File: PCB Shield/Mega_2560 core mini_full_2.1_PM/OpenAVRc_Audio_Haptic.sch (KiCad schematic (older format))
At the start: 13 parts, among them P22 JQ6500_28P, P27 HP, P5 Vibreur, P8 Audio

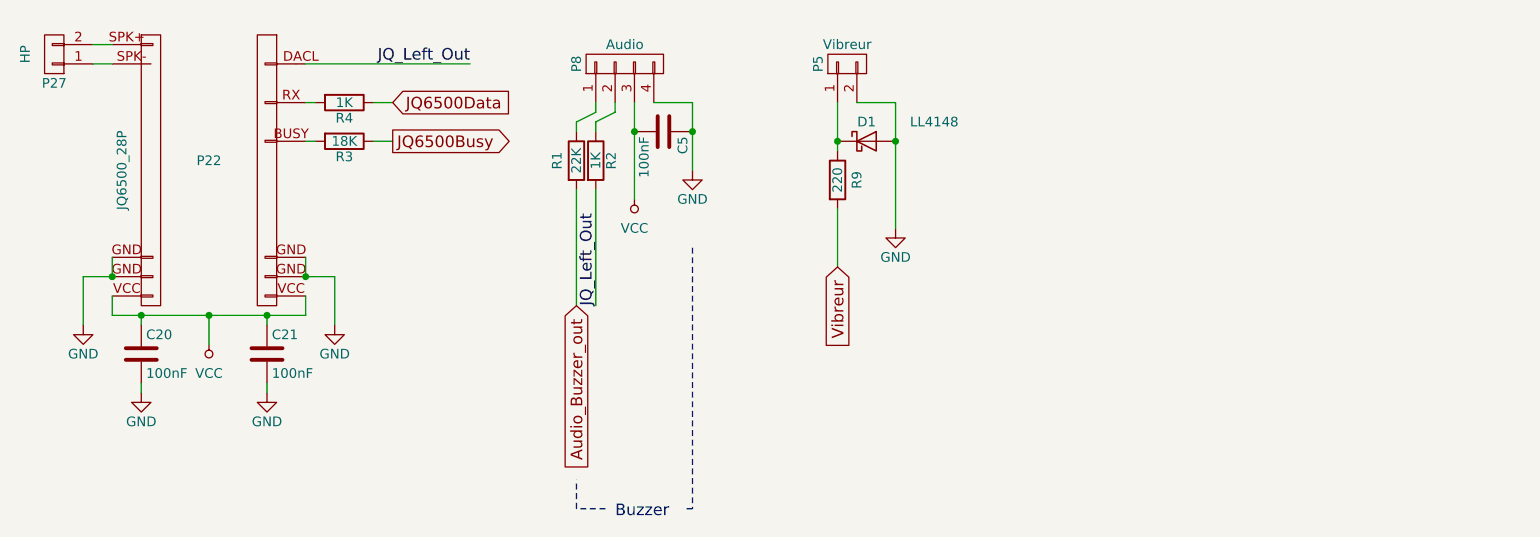
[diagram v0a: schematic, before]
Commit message: Update pcb files
update haptic pcb.
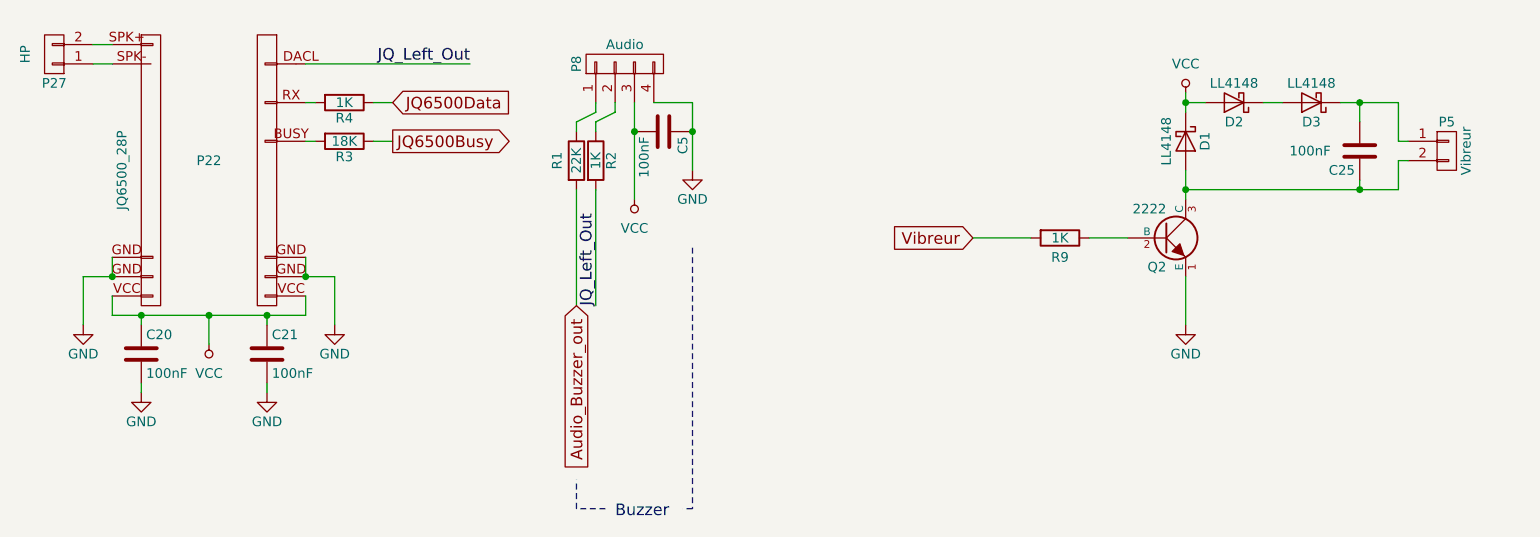
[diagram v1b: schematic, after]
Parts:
- added C25: 100nF, Capacitors_SMD:C_1206, symbol C-RESCUE-Mega_2560_core_mini_full_2.0
- added D2, D3: LL4148, Diodes_SMD:D_SOD-123, symbol MBR0520
- added Q2: 2222, symbol NPN
- R9: value 220 -> 1K
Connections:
- net GND: now also Q2.1 (E); no longer D1.2 (A), P5.2 (P2)
- net VCC: now also D1.1 (K), D2.2 (A)
- new net: C25.2, D3.1 (K), P5.1 (P1)
- new net: C25.1, D1.2 (A), P5.2 (P2), Q2.3 (C)
- new net: Q2.2 (B), R9.1
- new net: D2.1 (K), D3.2 (A)
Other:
- moved on the sheet: D1, P5, R9
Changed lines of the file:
@@
 Sheet 6 7
 Title "Shield Mega2560 core Full"
-Date "2018-02-28"
+Date "2018-03-01"
 Rev "2.10"
 Comp "© Team OpenAVRc"
@@
 L CONN_01X02 P5
 U 1 1 59C5A561
-P 7300 3050
-F 0 "P5" H 7300 3200 50  0000 C CNN
-F 1 "Vibreur" V 7400 3050 50  0000 C CNN
-F 2 "Pin_Headers:Pin_Header_Straight_1x02_Pitch2.54mm" H 7300 3050 50  0001 C CNN
-F 3 "" H 7300 3050 50  0000 C CNN
-	1    7300 3050
-	0    -1   -1   0
-$EndComp
-$Comp
-L GND-RESCUE-Mega_2560_core_mini_full_2.0 #PWR0105
-U 1 1 59C5A568
-P 7550 3900
-F 0 "#PWR0105" H 7550 3650 50  0001 C CNN
-F 1 "GND" H 7550 3750 50  0000 C CNN
-F 2 "" H 7550 3900 50  0000 C CNN
-F 3 "" H 7550 3900 50  0000 C CNN
-	1    7550 3900
+P 10400 3500
+F 0 "P5" H 10400 3650 50  0000 C CNN
+F 1 "Vibreur" V 10500 3500 50  0000 C CNN
+F 2 "Pin_Headers:Pin_Header_Straight_1x02_Pitch2.54mm" H 10400 3500 50  0001 C CNN
+F 3 "" H 10400 3500 50  0000 C CNN
+	1    10400 3500
 	1    0    0    -1
 $EndComp
@@
 $EndComp
 $Comp
-L VCC #PWR0106
+L VCC #PWR0105
 U 1 1 59C5A58E
 P 4000 4500
-F 0 "#PWR0106" H 4000 4350 50  0001 C CNN
+F 0 "#PWR0105" H 4000 4350 50  0001 C CNN
 F 1 "VCC" H 4000 4650 50  0000 C CNN
 F 2 "" H 4000 4500 50  0000 C CNN
@@
 $EndComp
 $Comp
-L GND-RESCUE-Mega_2560_core_mini_full_2.0 #PWR0107
+L GND-RESCUE-Mega_2560_core_mini_full_2.0 #PWR0106
 U 1 1 59C5A594
 P 3350 4400
-F 0 "#PWR0107" H 3350 4150 50  0001 C CNN
+F 0 "#PWR0106" H 3350 4150 50  0001 C CNN
 F 1 "GND" H 3350 4250 50  0000 C CNN
 F 2 "" H 3350 4400 50  0000 C CNN
@@
 $EndComp
 $Comp
-L GND-RESCUE-Mega_2560_core_mini_full_2.0 #PWR0108
+L GND-RESCUE-Mega_2560_core_mini_full_2.0 #PWR0107
 U 1 1 59C5A59A
 P 4650 4400
-F 0 "#PWR0108" H 4650 4150 50  0001 C CNN
+F 0 "#PWR0107" H 4650 4150 50  0001 C CNN
 F 1 "GND" H 4650 4250 50  0000 C CNN
 F 2 "" H 4650 4400 50  0000 C CNN
@@
 L MBR0520 D1
 U 1 1 59C5A5A7
-P 7400 3450
-F 0 "D1" H 7400 3550 50  0000 C CNN
-F 1 "LL4148" H 7750 3550 50  0000 C CNN
-F 2 "Diodes_SMD:D_SOD-123" H 7400 3275 50  0001 C CNN
-F 3 "" H 7400 3450 50  0001 C CNN
-	1    7400 3450
-	1    0    0    -1
+P 9050 3450
+F 0 "D1" H 9050 3550 50  0000 C CNN
+F 1 "LL4148" H 9050 3350 50  0000 C CNN
+F 2 "Diodes_SMD:D_SOD-123" H 9050 3275 50  0001 C CNN
+F 3 "" H 9050 3450 50  0001 C CNN
+	1    9050 3450
+	0    1    1    0
 $EndComp
 $Comp
 L R-RESCUE-Mega_2560_core_mini_full_2.0 R9
 U 1 1 59C5A5AE
-P 7250 3650
-F 0 "R9" V 7350 3650 50  0000 C CNN
-F 1 "220" V 7250 3650 50  0000 C CNN
-F 2 "anthoperso:R_1206" V 7180 3650 50  0001 C CNN
-F 3 "" H 7250 3650 50  0000 C CNN
-	1    7250 3650
-	1    0    0    -1
+P 8400 3950
+F 0 "R9" V 8500 3950 50  0000 C CNN
+F 1 "1K" V 8400 3950 50  0000 C CNN
+F 2 "anthoperso:R_1206" V 8330 3950 50  0001 C CNN
+F 3 "" H 8400 3950 50  0000 C CNN
+	1    8400 3950
+	0    1    1    0
 $EndComp
 $Comp
@@
 $EndComp
 $Comp
-L GND-RESCUE-Mega_2560_core_mini_full_2.0 #PWR0109
+L GND-RESCUE-Mega_2560_core_mini_full_2.0 #PWR0108
 U 1 1 59C5A5DF
 P 3650 4750
-F 0 "#PWR0109" H 3650 4500 50  0001 C CNN
+F 0 "#PWR0108" H 3650 4500 50  0001 C CNN
 F 1 "GND" H 3650 4600 50  0000 C CNN
 F 2 "" H 3650 4750 50  0000 C CNN
@@
 $EndComp
 $Comp
-L GND-RESCUE-Mega_2560_core_mini_full_2.0 #PWR0110
+L GND-RESCUE-Mega_2560_core_mini_full_2.0 #PWR0109
 U 1 1 59C5A5E5
 P 4300 4750
-F 0 "#PWR0110" H 4300 4500 50  0001 C CNN
+F 0 "#PWR0109" H 4300 4500 50  0001 C CNN
 F 1 "GND" H 4300 4600 50  0000 C CNN
 F 2 "" H 4300 4750 50  0000 C CNN
@@
 Wire Wire Line
 	6000 3700 6000 4300
-Connection ~ 7550 3450
-Wire Wire Line
-	7550 3250 7550 3900
-Wire Wire Line
-	7350 3250 7550 3250
 Connection ~ 6200 3400
 Connection ~ 6500 3400
@@
 	4500 3050 5350 3050
 Wire Wire Line
-	7250 3250 7250 3500
-Wire Wire Line
-	7250 3800 7250 4100
-Connection ~ 7250 3450
+	8250 3950 7950 3950
 Wire Wire Line
 	3400 3050 3500 3050
@@
 Text GLabel 4950 3450 2    60   Output ~ 0
 JQ6500Busy
-Text GLabel 7250 4100 3    60   Input ~ 0
+Text GLabel 7950 3950 0    60   Input ~ 0
 Vibreur
+$Comp
+L NPN Q2
+U 1 1 5A97FDE8
+P 8950 3950
+F 0 "Q2" H 8950 3800 50  0000 R CNN
+F 1 "2222" H 8950 4100 50  0000 R CNN
+F 2 "" H 8950 3950 60  0000 C CNN
+F 3 "" H 8950 3950 60  0000 C CNN
+	1    8950 3950
+	1    0    0    -1
+$EndComp
+Wire Wire Line
+	8550 3950 8750 3950
+$Comp
+L GND-RESCUE-Mega_2560_core_mini_full_2.0 #PWR0110
+U 1 1 5A9805CC
+P 9050 4400
+F 0 "#PWR0110" H 9050 4150 50  0001 C CNN
+F 1 "GND" H 9050 4250 50  0000 C CNN
+F 2 "" H 9050 4400 50  0000 C CNN
+F 3 "" H 9050 4400 50  0000 C CNN
+	1    9050 4400
+	1    0    0    -1
+$EndComp
+Wire Wire Line
+	9050 4150 9050 4400
+$Comp
+L C-RESCUE-Mega_2560_core_mini_full_2.0 C25
+U 1 1 5A980AA9
+P 9950 3500
+F 0 "C25" H 9975 3600 50  0000 L CNN
+F 1 "100nF" H 10100 3500 50  0000 L CNN
+F 2 "Capacitors_SMD:C_1206" H 9988 3350 50  0001 C CNN
+F 3 "" H 9950 3500 50  0000 C CNN
+	1    9950 3500
+	-1   0    0    1
+$EndComp
+$Comp
+L MBR0520 D2
+U 1 1 5A980F3A
+P 9300 3250
+F 0 "D2" H 9300 3350 50  0000 C CNN
+F 1 "LL4148" H 9300 3150 50  0000 C CNN
+F 2 "Diodes_SMD:D_SOD-123" H 9300 3075 50  0001 C CNN
+F 3 "" H 9300 3250 50  0001 C CNN
+	1    9300 3250
+	-1   0    0    1
+$EndComp
+$Comp
+L MBR0520 D3
+U 1 1 5A980F85
+P 9700 3250
+F 0 "D3" H 9700 3350 50  0000 C CNN
+F 1 "LL4148" H 9700 3150 50  0000 C CNN
+F 2 "Diodes_SMD:D_SOD-123" H 9700 3075 50  0001 C CNN
+F 3 "" H 9700 3250 50  0001 C CNN
+	1    9700 3250
+	-1   0    0    1
+$EndComp
+$Comp
+L VCC #PWR0111
+U 1 1 5A981097
+P 9050 3200
+F 0 "#PWR0111" H 9050 3050 50  0001 C CNN
+F 1 "VCC" H 9050 3350 50  0000 C CNN
+F 2 "" H 9050 3200 50  0000 C CNN
+F 3 "" H 9050 3200 50  0000 C CNN
+	1    9050 3200
+	1    0    0    -1
+$EndComp
+Wire Wire Line
+	9050 3200 9050 3300
+Wire Wire Line
+	9050 3750 9050 3600
+Wire Wire Line
+	9850 3250 10150 3250
+Wire Wire Line
+	9550 3250 9450 3250
+Wire Wire Line
+	9150 3250 9050 3250
+Connection ~ 9050 3250
+Wire Wire Line
+	10200 3450 10150 3450
+Wire Wire Line
+	10150 3450 10150 3250
+Wire Wire Line
+	9950 3350 9950 3250
+Connection ~ 9950 3250
+Wire Wire Line
+	10200 3550 10150 3550
+Wire Wire Line
+	10150 3550 10150 3700
+Wire Wire Line
+	10150 3700 9050 3700
+Connection ~ 9050 3700
+Wire Wire Line
+	9950 3650 9950 3700
+Connection ~ 9950 3700
 $EndSCHEMATC

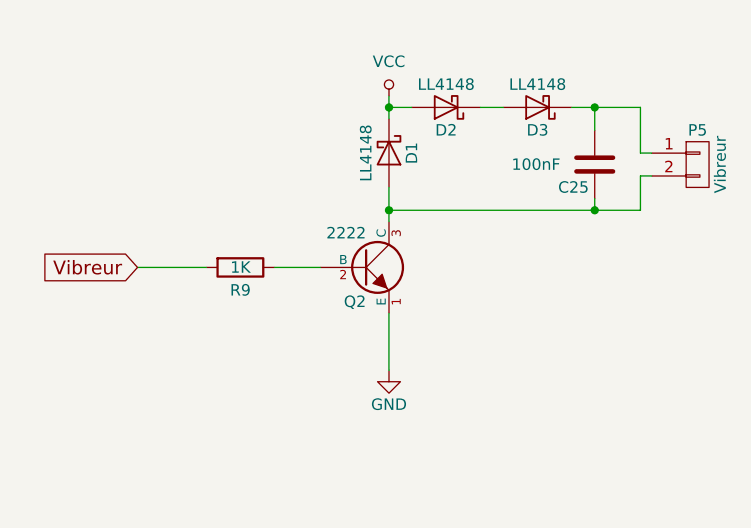
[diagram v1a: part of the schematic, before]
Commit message: Update schematic & pcb files
- modify pcb for haptic.
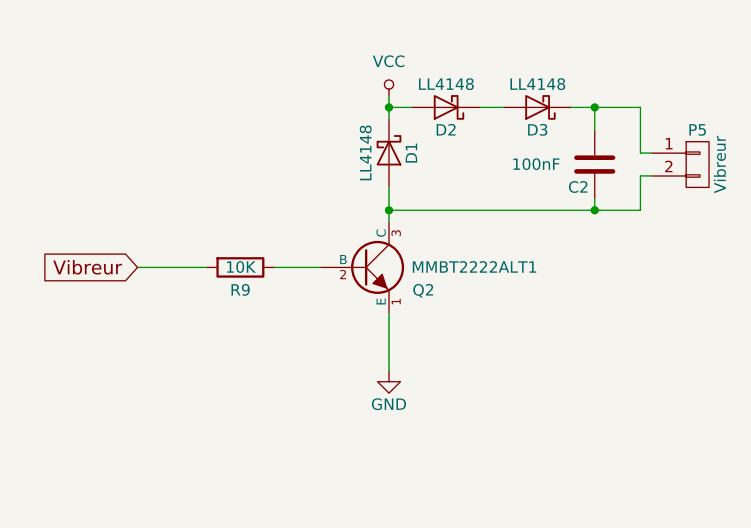
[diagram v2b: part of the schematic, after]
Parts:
- Q2: value 2222 -> MMBT2222ALT1
- R9: value 1K -> 10K
- renumbered C25 to C2
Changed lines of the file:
@@
 Sheet 6 7
 Title "Shield Mega2560 core Full"
-Date "2018-03-01"
+Date "2018-03-02"
 Rev "2.10"
 Comp "© Team OpenAVRc"
@@
 $EndDescr
 $Comp
-L GND-RESCUE-Mega_2560_core_mini_full_2.0 #PWR0103
+L GND-RESCUE-Mega_2560_core_mini_full_2.0 #PWR0102
 U 1 1 59C5A54C
 P 6500 3600
-F 0 "#PWR0103" H 6500 3350 50  0001 C CNN
+F 0 "#PWR0102" H 6500 3350 50  0001 C CNN
 F 1 "GND" H 6500 3450 50  0000 C CNN
 F 2 "" H 6500 3600 50  0000 C CNN
@@
 $EndComp
 $Comp
-L VCC #PWR0104
+L VCC #PWR0103
 U 1 1 59C5A552
 P 6200 3750
-F 0 "#PWR0104" H 6200 3600 50  0001 C CNN
+F 0 "#PWR0103" H 6200 3600 50  0001 C CNN
 F 1 "VCC" H 6200 3900 50  0000 C CNN
 F 2 "" H 6200 3750 50  0000 C CNN
@@
 $EndComp
 $Comp
-L VCC #PWR0105
+L VCC #PWR0104
 U 1 1 59C5A58E
 P 4000 4500
-F 0 "#PWR0105" H 4000 4350 50  0001 C CNN
+F 0 "#PWR0104" H 4000 4350 50  0001 C CNN
 F 1 "VCC" H 4000 4650 50  0000 C CNN
 F 2 "" H 4000 4500 50  0000 C CNN
@@
 $EndComp
 $Comp
-L GND-RESCUE-Mega_2560_core_mini_full_2.0 #PWR0106
+L GND-RESCUE-Mega_2560_core_mini_full_2.0 #PWR0105
 U 1 1 59C5A594
 P 3350 4400
-F 0 "#PWR0106" H 3350 4150 50  0001 C CNN
+F 0 "#PWR0105" H 3350 4150 50  0001 C CNN
 F 1 "GND" H 3350 4250 50  0000 C CNN
 F 2 "" H 3350 4400 50  0000 C CNN
@@
 $EndComp
 $Comp
-L GND-RESCUE-Mega_2560_core_mini_full_2.0 #PWR0107
+L GND-RESCUE-Mega_2560_core_mini_full_2.0 #PWR0106
 U 1 1 59C5A59A
 P 4650 4400
-F 0 "#PWR0107" H 4650 4150 50  0001 C CNN
+F 0 "#PWR0106" H 4650 4150 50  0001 C CNN
 F 1 "GND" H 4650 4250 50  0000 C CNN
 F 2 "" H 4650 4400 50  0000 C CNN
@@
 P 8400 3950
 F 0 "R9" V 8500 3950 50  0000 C CNN
-F 1 "1K" V 8400 3950 50  0000 C CNN
+F 1 "10K" V 8400 3950 50  0000 C CNN
 F 2 "anthoperso:R_1206" V 8330 3950 50  0001 C CNN
 F 3 "" H 8400 3950 50  0000 C CNN
@@
 $EndComp
 $Comp
-L GND-RESCUE-Mega_2560_core_mini_full_2.0 #PWR0108
+L GND-RESCUE-Mega_2560_core_mini_full_2.0 #PWR0107
 U 1 1 59C5A5DF
 P 3650 4750
-F 0 "#PWR0108" H 3650 4500 50  0001 C CNN
+F 0 "#PWR0107" H 3650 4500 50  0001 C CNN
 F 1 "GND" H 3650 4600 50  0000 C CNN
 F 2 "" H 3650 4750 50  0000 C CNN
@@
 $EndComp
 $Comp
-L GND-RESCUE-Mega_2560_core_mini_full_2.0 #PWR0109
+L GND-RESCUE-Mega_2560_core_mini_full_2.0 #PWR0108
 U 1 1 59C5A5E5
 P 4300 4750
-F 0 "#PWR0109" H 4300 4500 50  0001 C CNN
+F 0 "#PWR0108" H 4300 4500 50  0001 C CNN
 F 1 "GND" H 4300 4600 50  0000 C CNN
 F 2 "" H 4300 4750 50  0000 C CNN
 F 3 "" H 4300 4750 50  0000 C CNN
 	1    4300 4750
+	1    0    0    -1
+$EndComp
+Text GLabel 5900 4300 3    60   Input ~ 0
+Audio_Buzzer_out
+Text GLabel 4950 3250 2    60   Input ~ 0
+JQ6500Data
+Text GLabel 4950 3450 2    60   Output ~ 0
+JQ6500Busy
+Text GLabel 7950 3950 0    60   Input ~ 0
+Vibreur
+$Comp
+L NPN Q2
+U 1 1 5A97FDE8
+P 8950 3950
+F 0 "Q2" H 9250 3850 50  0000 R CNN
+F 1 "MMBT2222ALT1" H 9700 3950 50  0000 R CNN
+F 2 "" H 8950 3950 60  0000 C CNN
+F 3 "" H 8950 3950 60  0000 C CNN
+	1    8950 3950
+	1    0    0    -1
+$EndComp
+$Comp
+L GND-RESCUE-Mega_2560_core_mini_full_2.0 #PWR0109
+U 1 1 5A9805CC
+P 9050 4400
+F 0 "#PWR0109" H 9050 4150 50  0001 C CNN
+F 1 "GND" H 9050 4250 50  0000 C CNN
+F 2 "" H 9050 4400 50  0000 C CNN
+F 3 "" H 9050 4400 50  0000 C CNN
+	1    9050 4400
+	1    0    0    -1
+$EndComp
+$Comp
+L C-RESCUE-Mega_2560_core_mini_full_2.0 C2
+U 1 1 5A980AA9
+P 9950 3500
+F 0 "C2" H 9975 3600 50  0000 L CNN
+F 1 "100nF" H 10100 3500 50  0000 L CNN
+F 2 "Capacitors_SMD:C_1206" H 9988 3350 50  0001 C CNN
+F 3 "" H 9950 3500 50  0000 C CNN
+	1    9950 3500
+	-1   0    0    1
+$EndComp
+$Comp
+L MBR0520 D2
+U 1 1 5A980F3A
+P 9300 3250
+F 0 "D2" H 9300 3350 50  0000 C CNN
+F 1 "LL4148" H 9300 3150 50  0000 C CNN
+F 2 "Diodes_SMD:D_SOD-123" H 9300 3075 50  0001 C CNN
+F 3 "" H 9300 3250 50  0001 C CNN
+	1    9300 3250
+	-1   0    0    1
+$EndComp
+$Comp
+L MBR0520 D3
+U 1 1 5A980F85
+P 9700 3250
+F 0 "D3" H 9700 3350 50  0000 C CNN
+F 1 "LL4148" H 9700 3150 50  0000 C CNN
+F 2 "Diodes_SMD:D_SOD-123" H 9700 3075 50  0001 C CNN
+F 3 "" H 9700 3250 50  0001 C CNN
+	1    9700 3250
+	-1   0    0    1
+$EndComp
+$Comp
+L VCC #PWR0110
+U 1 1 5A981097
+P 9050 3200
+F 0 "#PWR0110" H 9050 3050 50  0001 C CNN
+F 1 "VCC" H 9050 3350 50  0000 C CNN
+F 2 "" H 9050 3200 50  0000 C CNN
+F 3 "" H 9050 3200 50  0000 C CNN
+	1    9050 3200
 	1    0    0    -1
 $EndComp
@@
 Wire Wire Line
 	3650 4700 3650 4750
-Text GLabel 5900 4300 3    60   Input ~ 0
-Audio_Buzzer_out
-Text GLabel 4950 3250 2    60   Input ~ 0
-JQ6500Data
-Text GLabel 4950 3450 2    60   Output ~ 0
-JQ6500Busy
-Text GLabel 7950 3950 0    60   Input ~ 0
-Vibreur
-$Comp
-L NPN Q2
-U 1 1 5A97FDE8
-P 8950 3950
-F 0 "Q2" H 8950 3800 50  0000 R CNN
-F 1 "2222" H 8950 4100 50  0000 R CNN
-F 2 "" H 8950 3950 60  0000 C CNN
-F 3 "" H 8950 3950 60  0000 C CNN
-	1    8950 3950
-	1    0    0    -1
-$EndComp
 Wire Wire Line
 	8550 3950 8750 3950
-$Comp
-L GND-RESCUE-Mega_2560_core_mini_full_2.0 #PWR0110
-U 1 1 5A9805CC
-P 9050 4400
-F 0 "#PWR0110" H 9050 4150 50  0001 C CNN
-F 1 "GND" H 9050 4250 50  0000 C CNN
-F 2 "" H 9050 4400 50  0000 C CNN
-F 3 "" H 9050 4400 50  0000 C CNN
-	1    9050 4400
-	1    0    0    -1
-$EndComp
 Wire Wire Line
 	9050 4150 9050 4400
-$Comp
-L C-RESCUE-Mega_2560_core_mini_full_2.0 C25
-U 1 1 5A980AA9
-P 9950 3500
-F 0 "C25" H 9975 3600 50  0000 L CNN
-F 1 "100nF" H 10100 3500 50  0000 L CNN
-F 2 "Capacitors_SMD:C_1206" H 9988 3350 50  0001 C CNN
-F 3 "" H 9950 3500 50  0000 C CNN
-	1    9950 3500
-	-1   0    0    1
-$EndComp
-$Comp
-L MBR0520 D2
-U 1 1 5A980F3A
-P 9300 3250
-F 0 "D2" H 9300 3350 50  0000 C CNN
-F 1 "LL4148" H 9300 3150 50  0000 C CNN
-F 2 "Diodes_SMD:D_SOD-123" H 9300 3075 50  0001 C CNN
-F 3 "" H 9300 3250 50  0001 C CNN
-	1    9300 3250
-	-1   0    0    1
-$EndComp
-$Comp
-L MBR0520 D3
-U 1 1 5A980F85
-P 9700 3250
-F 0 "D3" H 9700 3350 50  0000 C CNN
-F 1 "LL4148" H 9700 3150 50  0000 C CNN
-F 2 "Diodes_SMD:D_SOD-123" H 9700 3075 50  0001 C CNN
-F 3 "" H 9700 3250 50  0001 C CNN
-	1    9700 3250
-	-1   0    0    1
-$EndComp
-$Comp
-L VCC #PWR0111
-U 1 1 5A981097
-P 9050 3200
-F 0 "#PWR0111" H 9050 3050 50  0001 C CNN
-F 1 "VCC" H 9050 3350 50  0000 C CNN
-F 2 "" H 9050 3200 50  0000 C CNN
-F 3 "" H 9050 3200 50  0000 C CNN
-	1    9050 3200
-	1    0    0    -1
-$EndComp
 Wire Wire Line
 	9050 3200 9050 3300

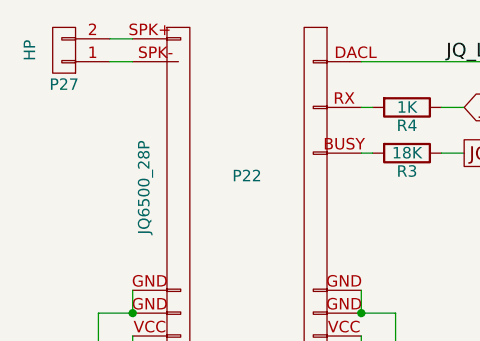
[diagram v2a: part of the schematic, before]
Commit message: Update schematic & pcb files
-remove P27.
-clean hold_power signal.
-add G3,H7 and G4 pins as dummy pins on 3 pins connector.
-update schematic.
-remove package errors in pcbnew.
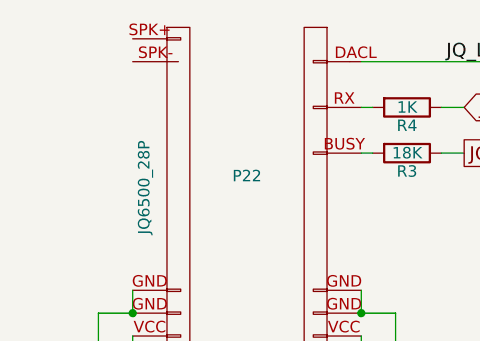
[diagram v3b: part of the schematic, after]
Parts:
- removed P27: HP, Pin_Headers:Pin_Header_Straight_1x02_Pitch2.54mm, symbol CONN_01X02
- Q2: footprint (none) -> SOT-23_MMBT2222
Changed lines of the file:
@@
 Sheet 6 7
 Title "Shield Mega2560 core Full"
-Date "2018-03-02"
+Date "2018-03-06"
 Rev "2.10"
 Comp "© Team OpenAVRc"
@@
 	1    8400 3950
 	0    1    1    0
-$EndComp
-$Comp
-L CONN_01X02 P27
-U 1 1 59C5A5B5
-P 3200 3000
-F 0 "P27" H 3200 3150 50  0000 C CNN
-F 1 "HP" V 3350 3000 50  0000 C CNN
-F 2 "Pin_Headers:Pin_Header_Straight_1x02_Pitch2.54mm" H 3200 3000 50  0001 C CNN
-F 3 "" H 3200 3000 50  0000 C CNN
-	1    3200 3000
-	-1   0    0    1
 $EndComp
 $Comp
@@
 F 0 "Q2" H 9250 3850 50  0000 R CNN
 F 1 "MMBT2222ALT1" H 9700 3950 50  0000 R CNN
-F 2 "" H 8950 3950 60  0000 C CNN
+F 2 "SOT-23_MMBT2222" H 8950 3950 60  0001 C CNN
 F 3 "" H 8950 3950 60  0000 C CNN
 	1    8950 3950
@@
 	8250 3950 7950 3950
 Wire Wire Line
-	3400 3050 3500 3050
-Wire Wire Line
-	3500 2950 3400 2950
-Wire Wire Line
 	6000 3400 6000 3350
